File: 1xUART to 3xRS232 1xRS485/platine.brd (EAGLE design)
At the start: 86.5 x 53.5 mm, 25 parts, among them IC1 74ALS08D, IC2 74ALS08D, IC3 MAX3232CSE, IC4 MAX3232CSE, IC5 MAX3232CSE, IC6 MAX481CSA

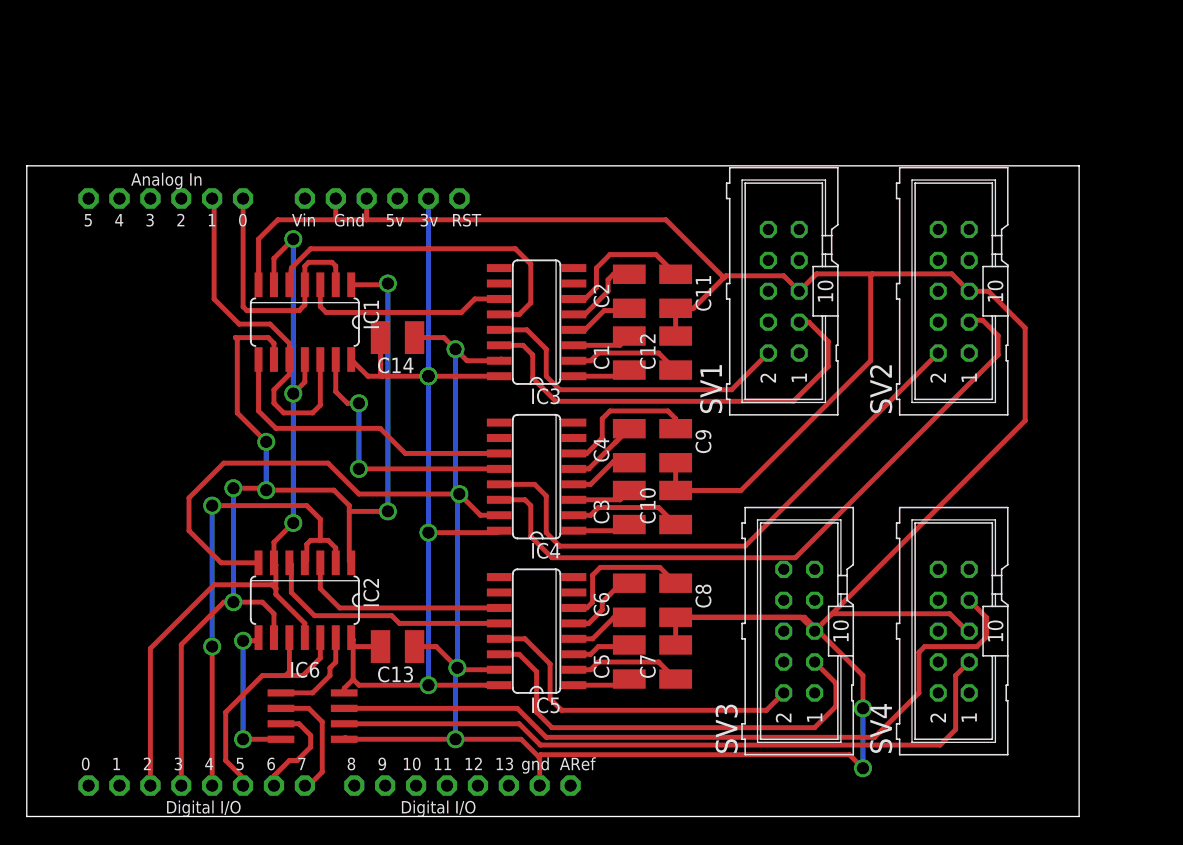
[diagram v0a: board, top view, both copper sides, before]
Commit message: redesign for etching
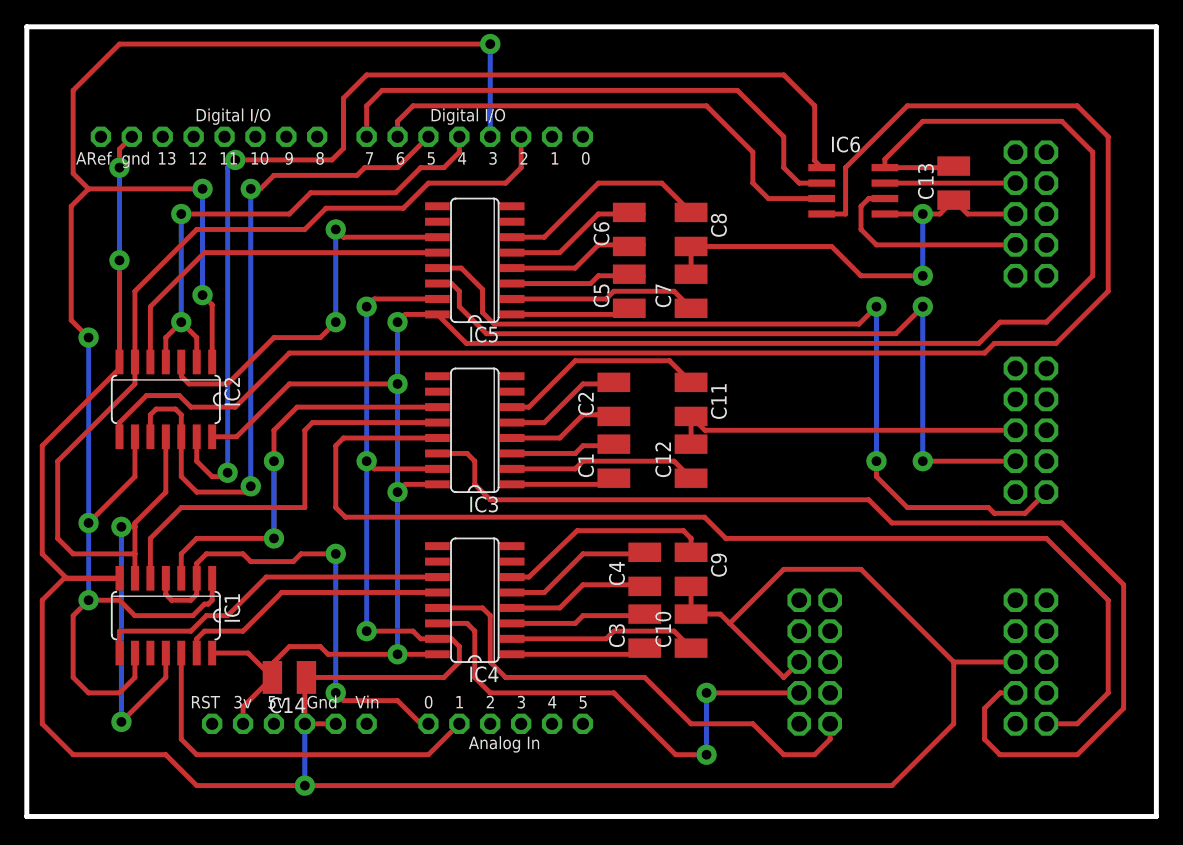
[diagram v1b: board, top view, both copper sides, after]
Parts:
- moved U$1 98.9 mm to (-17.8, 5.08), turned to 0 degrees
- moved IC6 62.0 mm to (67.9, 51.4)
- moved C13 59.5 mm to (76.2, 52.1), turned to 90 degrees
- moved SV1 36.6 mm to (82.5, 12.7), flipped to the bottom
- moved SV4 34.9 mm to (82.5, 49.5), flipped to the bottom
- moved SV2 32.6 mm to (64.8, 12.7), flipped to the bottom
- moved IC5 30.9 mm to (36.8, 45.7)
- moved C7 30.5 mm to (54.6, 43.2)
- moved C8 30.5 mm to (54.6, 48.3)
- moved C5 30.5 mm to (49.5, 43.2)
- moved C6 30.5 mm to (49.5, 48.3)
- moved C14 29.3 mm to (21.6, 11.4)
- moved IC1 26.7 mm to (11.4, 16.5)
- moved SV3 25.2 mm to (82.5, 31.8), flipped to the bottom
- moved IC2 20.1 mm to (11.4, 34.3)
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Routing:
- net N$7: track 12.6 -> 130.9 mm, vias 2 -> 0
- net P3V3: track 82.3 -> 170.7 mm
- net N$8: track 7.94 -> 90.5 mm, vias 0 -> 2
- net RX1: track 26.7 -> 94.1 mm
- net TX: track 90.5 -> 147.7 mm
- net TX1: track 36.4 -> 91.3 mm
- net D-: track 62.8 -> 10.7 mm
- net RX3: track 28.1 -> 69.6 mm, vias 0 -> 2
- net D+: track 57.5 -> 17.4 mm
- net RX: track 66.0 -> 105.3 mm, vias 3 -> 2
- net EN4: track 21.2 -> 57.1 mm, vias 0 -> 2
- net RE: track 9.87 -> 45.1 mm
- net WE: track 8.58 -> 41.3 mm
- net TX3: track 37.2 -> 63.6 mm, vias 0 -> 2
- net EN1: track 21.8 -> 39.2 mm, vias 0 -> 2
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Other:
- board size 86.5 x 53.5 mm -> 92.9 x 64.9 mm
